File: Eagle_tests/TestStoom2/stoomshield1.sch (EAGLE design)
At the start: 2 parts

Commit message: Hardware test: eagle file with TFT-Due connectors + relay buffer
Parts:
- added IC1: 74HC245N, 74xx-eu:74HC245N
- added JP1: (no value), jumper:JP2E
- added JP2: (no value), pinhead:PINHD-1X8
- added RELAYS1, RELAYS2: (no value), pinhead:PINHD-1X6
- added RN1: (no value), resistor-sil:G08R
- added SV1, SV2, SV3: (no value), con-lsta:FE10-1
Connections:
- new net KLEP1: IC1A.B1, RELAYS1.2
- new net KLEP1_SIG: IC1A.A1, JP2.1, RN1.9
- new net KLEP2: IC1A.B2, RELAYS1.3
- new net KLEP2_SIG: IC1A.A2, JP2.2, RN1.8
- new net KLEP3: IC1A.B3, RELAYS1.4
- new net KLEP3_SIG: IC1A.A3, JP2.3, RN1.7
- new net KLEP4: IC1A.B4, RELAYS1.5
- new net KLEP4_SIG: IC1A.A4, JP2.4, RN1.6
- new net KLEP5: IC1A.B5, RELAYS2.2
- new net KLEP5_SIG: IC1A.A5, JP2.5, RN1.5
- new net KLEP6: IC1A.B6, RELAYS2.3
- new net KLEP6_SIG: IC1A.A6, JP2.6, RN1.4
- new net KLEP7: IC1A.B7, RELAYS2.4
- new net KLEP7_SIG: IC1A.A7, JP2.7, RN1.3
- new net KLEP8: IC1A.B8, RELAYS2.5
- new net KLEP8_SIG: IC1A.A8, JP2.8, RN1.2
- new net N$1: JP1.2, TFT-3.S
- net GND: now also IC1A.G, IC1P.GND, RELAYS1.6, RELAYS2.6, SV1.1, SV1.10, SV1.2, SV1.3, SV1.4, SV1.5, SV1.6, SV1.7, SV1.8, SV1.9
- net VCC: now also IC1A.DIR, IC1P.VCC, JP1.1, JP1.3, RELAYS1.1, RELAYS2.1, RN1.1, SV2.1, SV2.10, SV2.2, SV2.3, SV2.4, SV2.5, SV2.6, SV2.7, SV2.8, SV2.9, SV3.1, SV3.10, SV3.2, SV3.3, SV3.4, SV3.5, SV3.6, SV3.7, SV3.8, SV3.9; no longer TFT-3.S
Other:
- moved on the sheet: DUED-1, DUED-10, DUED-11, DUED-12, DUED-13, DUED-14, DUED-15, DUED-16, DUED-17, DUED-18, DUED-19, DUED-2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

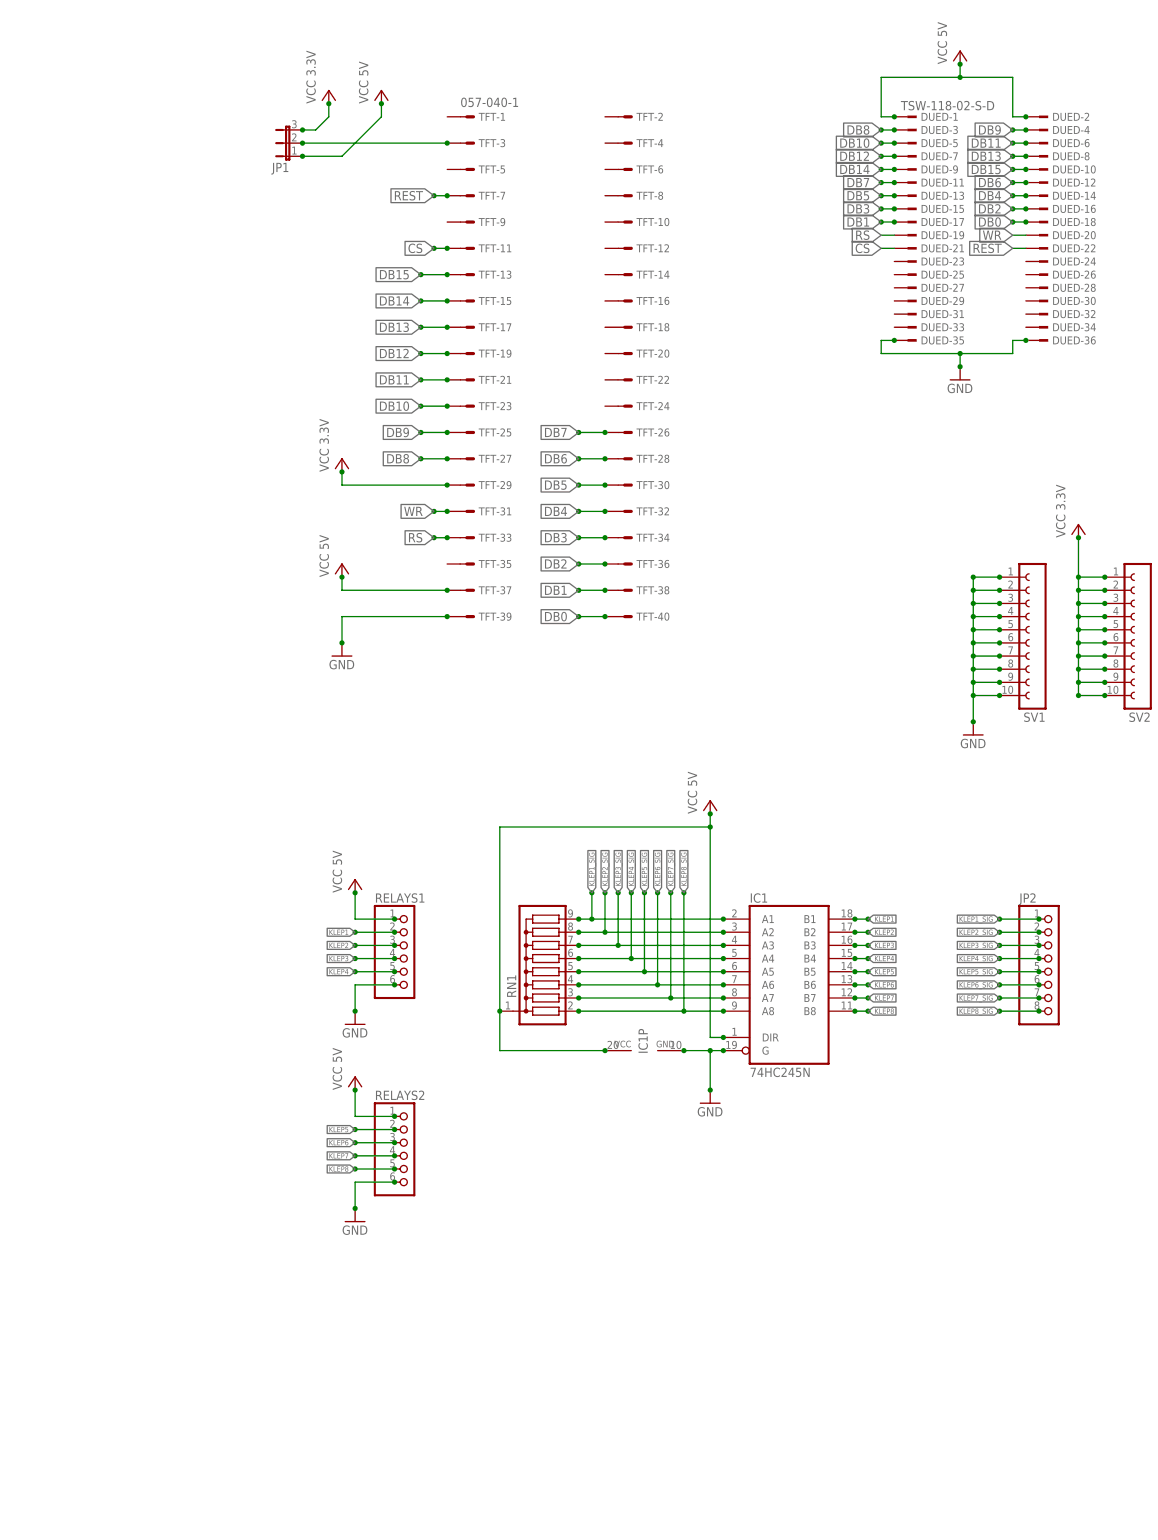
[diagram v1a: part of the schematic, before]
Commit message: Hardware test: eagle file with TFT-Due connectors + relay buffer + sensor optocoupler
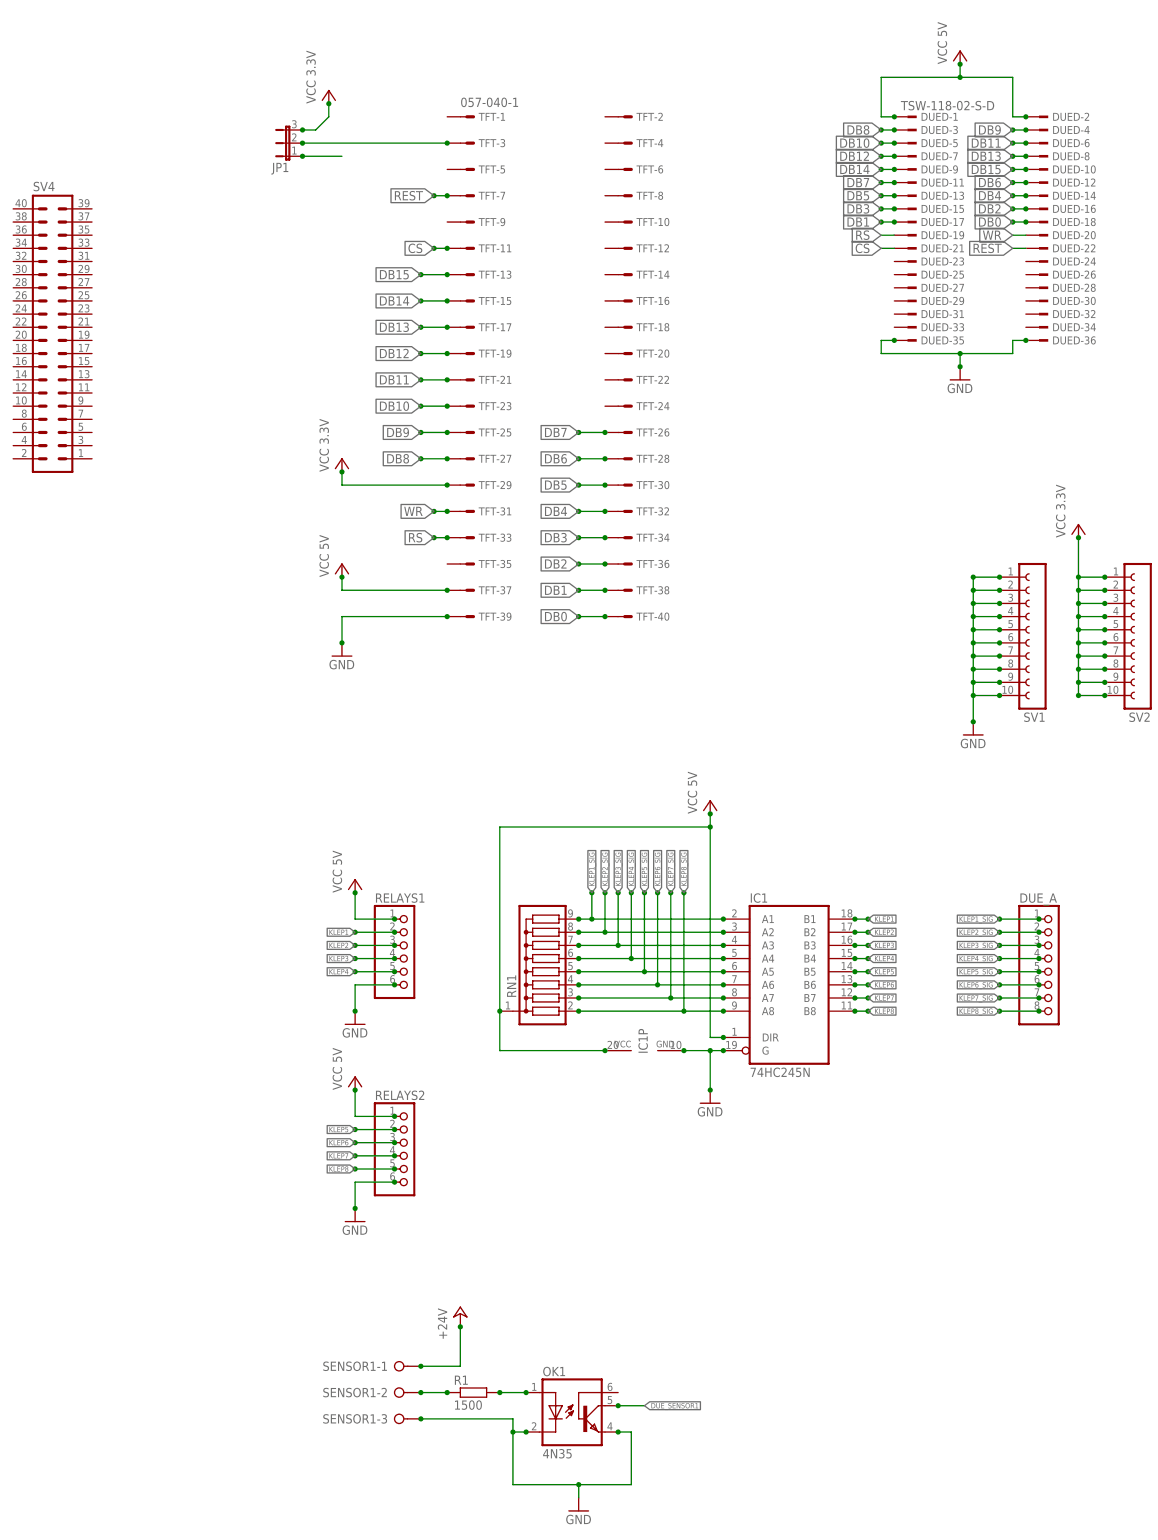
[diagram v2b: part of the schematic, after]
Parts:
- added OK1: 4N35, optocoupler:4N35
- added R1: 1500, resistor:R-EU_0207/5V
- added SENSOR1: (no value), con-wago-508:W237-03P
- added SV4: (no value), con-harting-ml:ML40
- renumbered JP2 to DUE_A
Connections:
- new net +24V: SENSOR1-1.KL
- new net DUE_SENSOR1: OK1.COL
- new net N$2: JP1.1
- new net N$3: R1.1, SENSOR1-2.KL
- new net N$4: OK1.A, R1.2
- net GND: now also OK1.C, OK1.EMI, SENSOR1-3.KL
- net VCC: no longer JP1.1

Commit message: Hardware test: eagle schema details
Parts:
- removed SV4: (no value), con-harting-ml:ML40
- added JP2: (no value), jumper:JP1Q
- added LED1, LED2, LED3, LED4: (no value), led:LED5MM
- added OK2, OK3, OK4: 4N35, optocoupler:4N35
- added PL1: (no value), con-harting-v:40V
- added R2, R4, R6, R8: (no value), resistor:R-EU_0204/5
- added R3, R5, R7: 1500, resistor:R-EU_0207/5V
- added SENSOR2, SENSOR3, SENSOR4: (no value), con-wago-508:W237-03P
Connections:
- removed net VCC: DUED-1.1, DUED-2.1, IC1A.DIR, IC1P.VCC, JP1.3, RELAYS1.1, RELAYS2.1, RN1.1, SV2.1, SV2.10, SV2.2, SV2.3, SV2.4, SV2.5, SV2.6, SV2.7, SV2.8, SV2.9, SV3.1, SV3.10, SV3.2, SV3.3, SV3.4, SV3.5, SV3.6, SV3.7, SV3.8, SV3.9, TFT-29.S, TFT-37.S
- new net +3V3: JP1.3, SV2.1, SV2.10, SV2.2, SV2.3, SV2.4, SV2.5, SV2.6, SV2.7, SV2.8, SV2.9, TFT-29.S
- new net +5V: DUED-1.1, DUED-2.1, IC1A.DIR, IC1P.VCC, R2.1, R4.1, R6.1, R8.1, RELAYS1.1, RELAYS2.1, RN1.1, SV3.1, SV3.10, SV3.2, SV3.3, SV3.4, SV3.5, SV3.6, SV3.7, SV3.8, SV3.9, TFT-37.S
- new net DUE_SENSOR2: LED2.A, OK2.COL
- new net DUE_SENSOR3: LED3.A, OK3.COL
- new net DUE_SENSOR4: LED4.A, OK4.COL
- new net GND1: JP2.2, OK1.C, OK2.C, OK3.C, OK4.C, SENSOR1-3.KL, SENSOR2-3.KL, SENSOR3-3.KL, SENSOR4-3.KL
- new net N$10: R5.1, SENSOR3-2.KL
- new net N$11: LED3.C, R6.2
- new net N$12: OK4.A, R7.2
- new net N$13: R7.1, SENSOR4-2.KL
- new net N$14: LED4.C, R8.2
- new net N$5: LED1.C, R2.2
- new net N$6: OK2.A, R3.2
- new net N$7: R3.1, SENSOR2-2.KL
- new net N$8: LED2.C, R4.2
- new net N$9: OK3.A, R5.2
- net +24V: now also SENSOR2-1.KL, SENSOR3-1.KL, SENSOR4-1.KL
- net DUE_SENSOR1: now also LED1.A
- net GND: now also JP2.1, OK2.EMI, OK3.EMI, OK4.EMI; no longer OK1.C, SENSOR1-3.KL
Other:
- moved on the sheet: OK1, R1, SENSOR1-1, SENSOR1-2, SENSOR1-3

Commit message: Hardware test: improved eagle pcb (100x80mm) with sensor leds.
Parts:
- removed PL1: (no value), con-harting-v:40V
- removed SV1, SV2, SV3: (no value), con-lsta:FE10-1
- added R10, R11, R12, R9: 10000, resistor:R-EU_0204/5
- added SENSOR_PWR: (no value), con-wago-508:W237-02P
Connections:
- net +24V: now also SENSOR_PWR-2.KL
- net +3V3: no longer SV2.1, SV2.10, SV2.2, SV2.3, SV2.4, SV2.5, SV2.6, SV2.7, SV2.8, SV2.9
- net +5V: now also R10.1, R11.1, R12.1, R2.2, R9.1; no longer R2.1, SV3.1, SV3.10, SV3.2, SV3.3, SV3.4, SV3.5, SV3.6, SV3.7, SV3.8, SV3.9
- net DUE_SENSOR1: now also R9.2
- net DUE_SENSOR2: now also R10.2
- net DUE_SENSOR3: now also R11.2
- net DUE_SENSOR4: now also R12.2
- net GND: no longer SV1.1, SV1.10, SV1.2, SV1.3, SV1.4, SV1.5, SV1.6, SV1.7, SV1.8, SV1.9
- net GND1: now also SENSOR_PWR-1.KL
- net N$5: now also R2.1; no longer R2.2
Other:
- moved on the sheet: JP2, LED1, LED2, LED3, LED4, OK2, OK3, OK4, R2, R3, R4, R5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

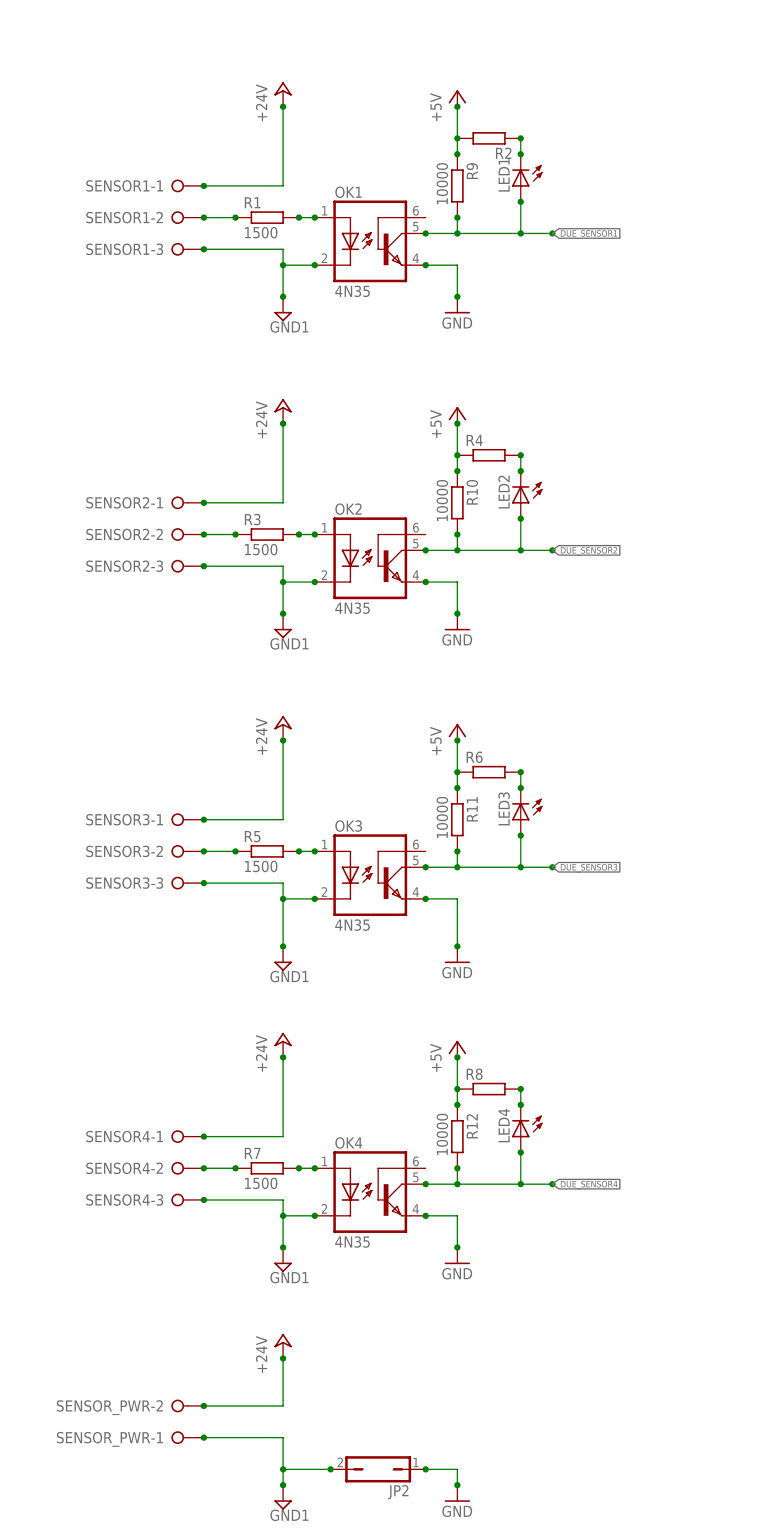
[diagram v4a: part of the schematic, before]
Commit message: Hardware test: improved eagle pcb screw contact wiring.
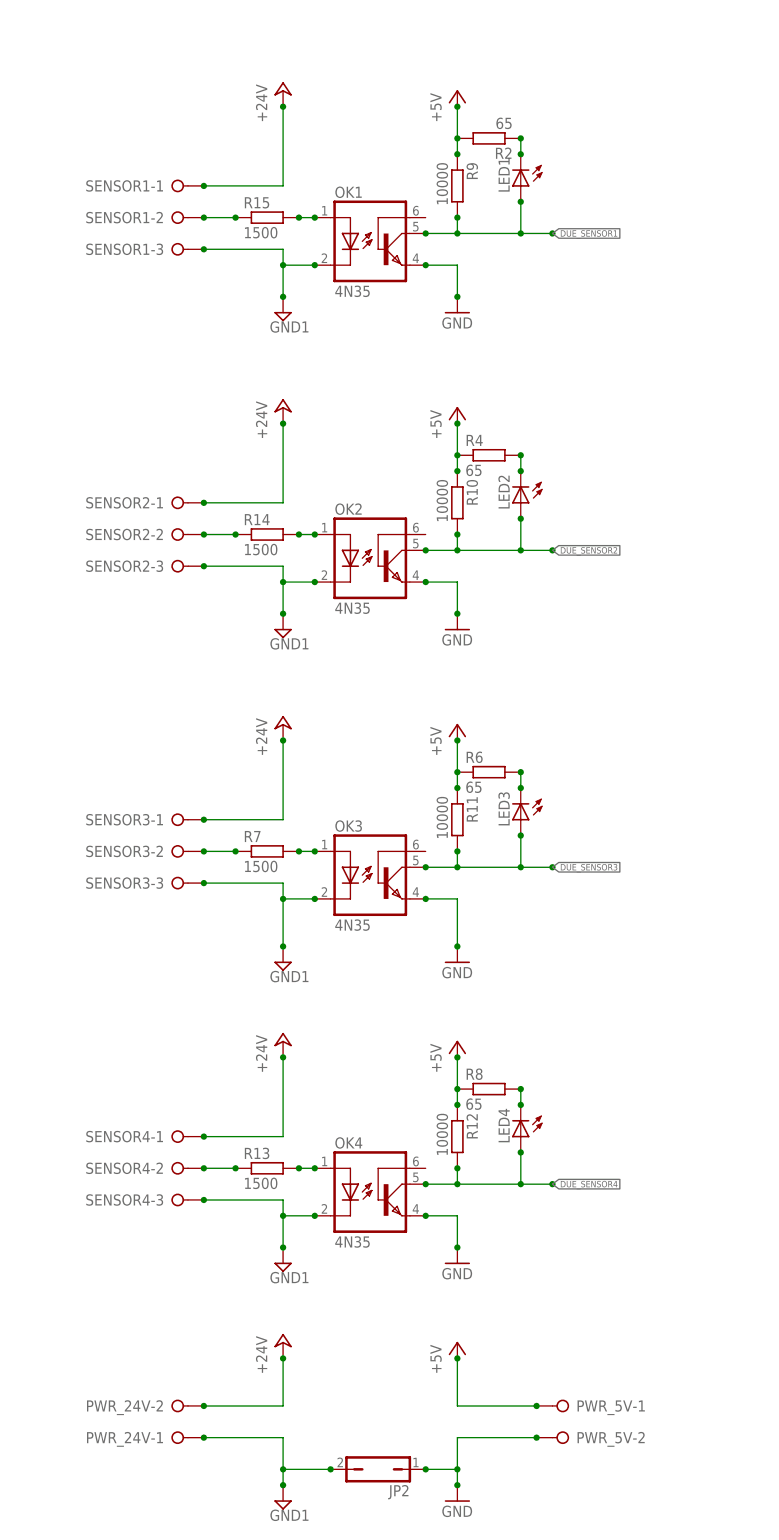
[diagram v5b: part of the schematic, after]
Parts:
- removed R1, R3, R5: 1500, resistor:R-EU_0207/5V
- added PWR_5V: (no value), con-wago-508:W237-02P
- added R13, R14, R15: 1500, resistor:R-EU_0204/5
- R2, R4, R6, R8: value (none) -> 65
- R7: device resistor:R-EU_0207/5V -> resistor:R-EU_0204/5
- renumbered SENSOR_PWR to PWR_24V
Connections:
- net +5V: now also PWR_5V-1.KL
- net GND: now also PWR_5V-2.KL
- net N$10: now also R7.1; no longer R5.1
- net N$12: now also R13.2; no longer R7.2
- net N$13: now also R13.1; no longer R7.1
- net N$3: now also R15.1; no longer R1.1
- net N$4: now also R15.2; no longer R1.2
- net N$6: now also R14.2; no longer R3.2
- net N$7: now also R14.1; no longer R3.1
- net N$9: now also R7.2; no longer R5.2
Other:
- moved on the sheet: R7
